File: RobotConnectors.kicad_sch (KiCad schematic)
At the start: 87 parts, among them J1 Conn_02x11_Top_Bottom, J10 Conn_01x05, J11 SA/SC Perimeter Plug, J12 Hall3 (Lift Left), J13 Hall2 (Lift Right), J14 Hall1 (Stop1), J15 Hall0 (Stop2), J17 Conn_01x02, J18 Conn_01x02, J19 Conn_01x04, J2 Conn_02x04_Top_Bottom, J21 Conn_01x05, J27 Rear Stop Switch 2, J3 Conn_01x02, J4 Conn_01x04, J40 Rear Stop Switch 1, J5 OEM CoverUI, J6 Conn_01x14_Socket, J7 USS 1-5, J8 Hall5 (Lift Left 2), J9 Hall4 (Lift Right 2), U11 SN74LVC07ADBR, U12 SN74LVC07ADBR, U14 Fuse Holder, U15 Fuse Holder, U16 Fuse Holder, U17 Fuse Holder, U2 TPS2065CDBV, U28 Fuse 2A, U29 Fuse 2A, U47 SN74LVC157ADR, U48 SN74LVC157ADR

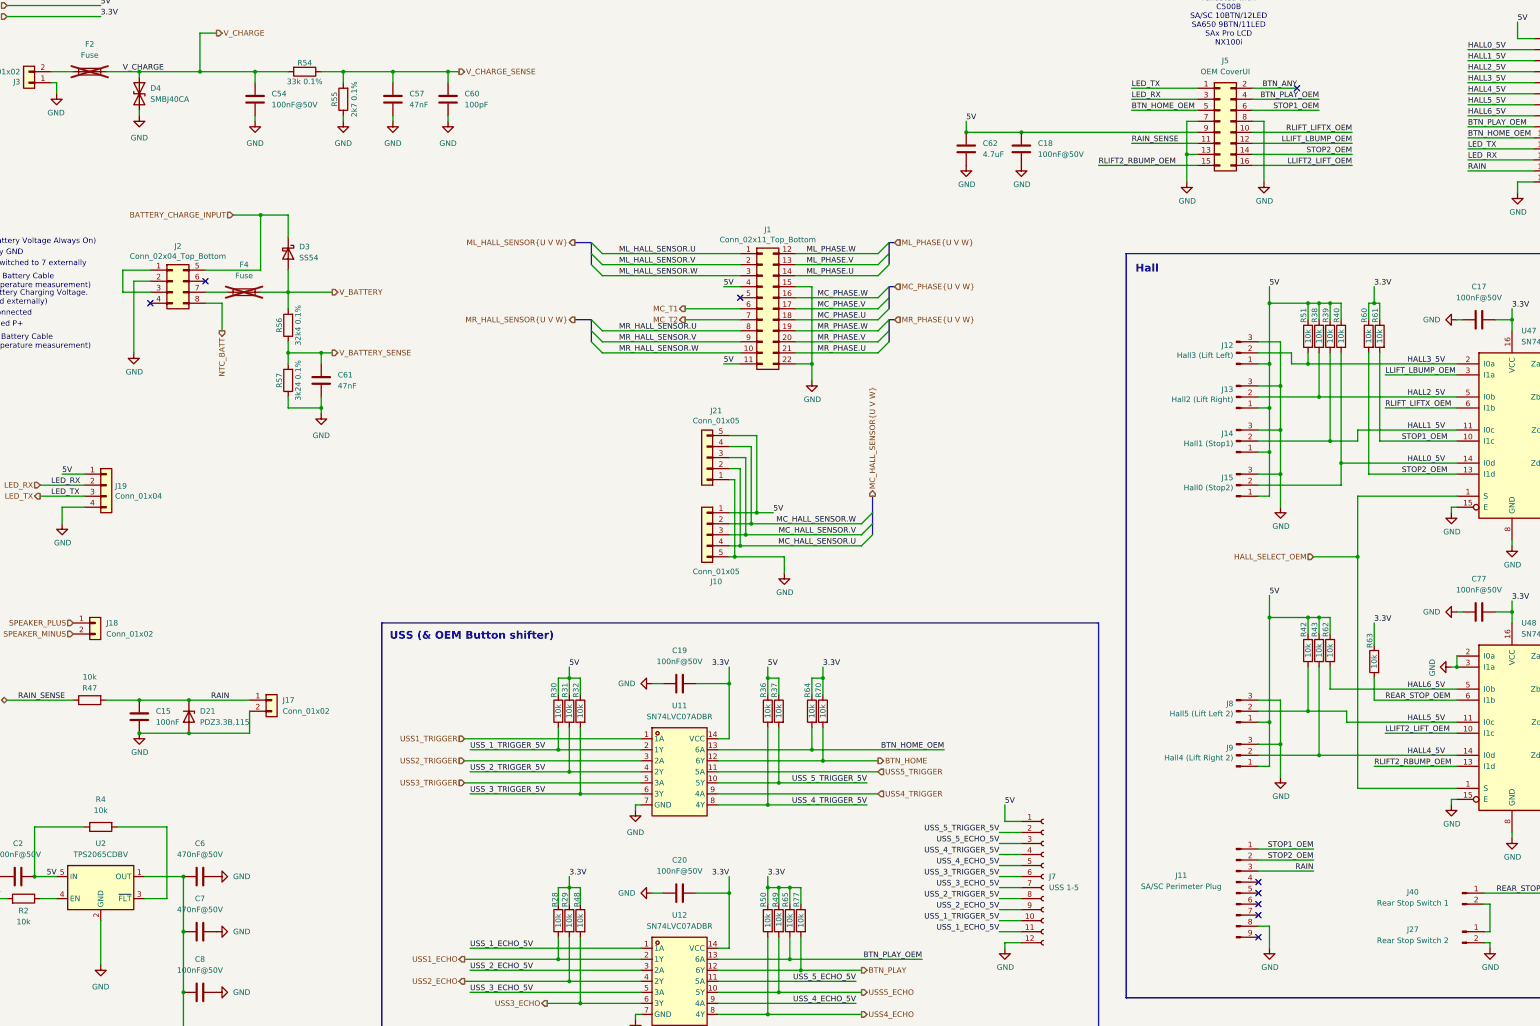
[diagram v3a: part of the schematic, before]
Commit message: Fix BOM and switch C0402 to C0603
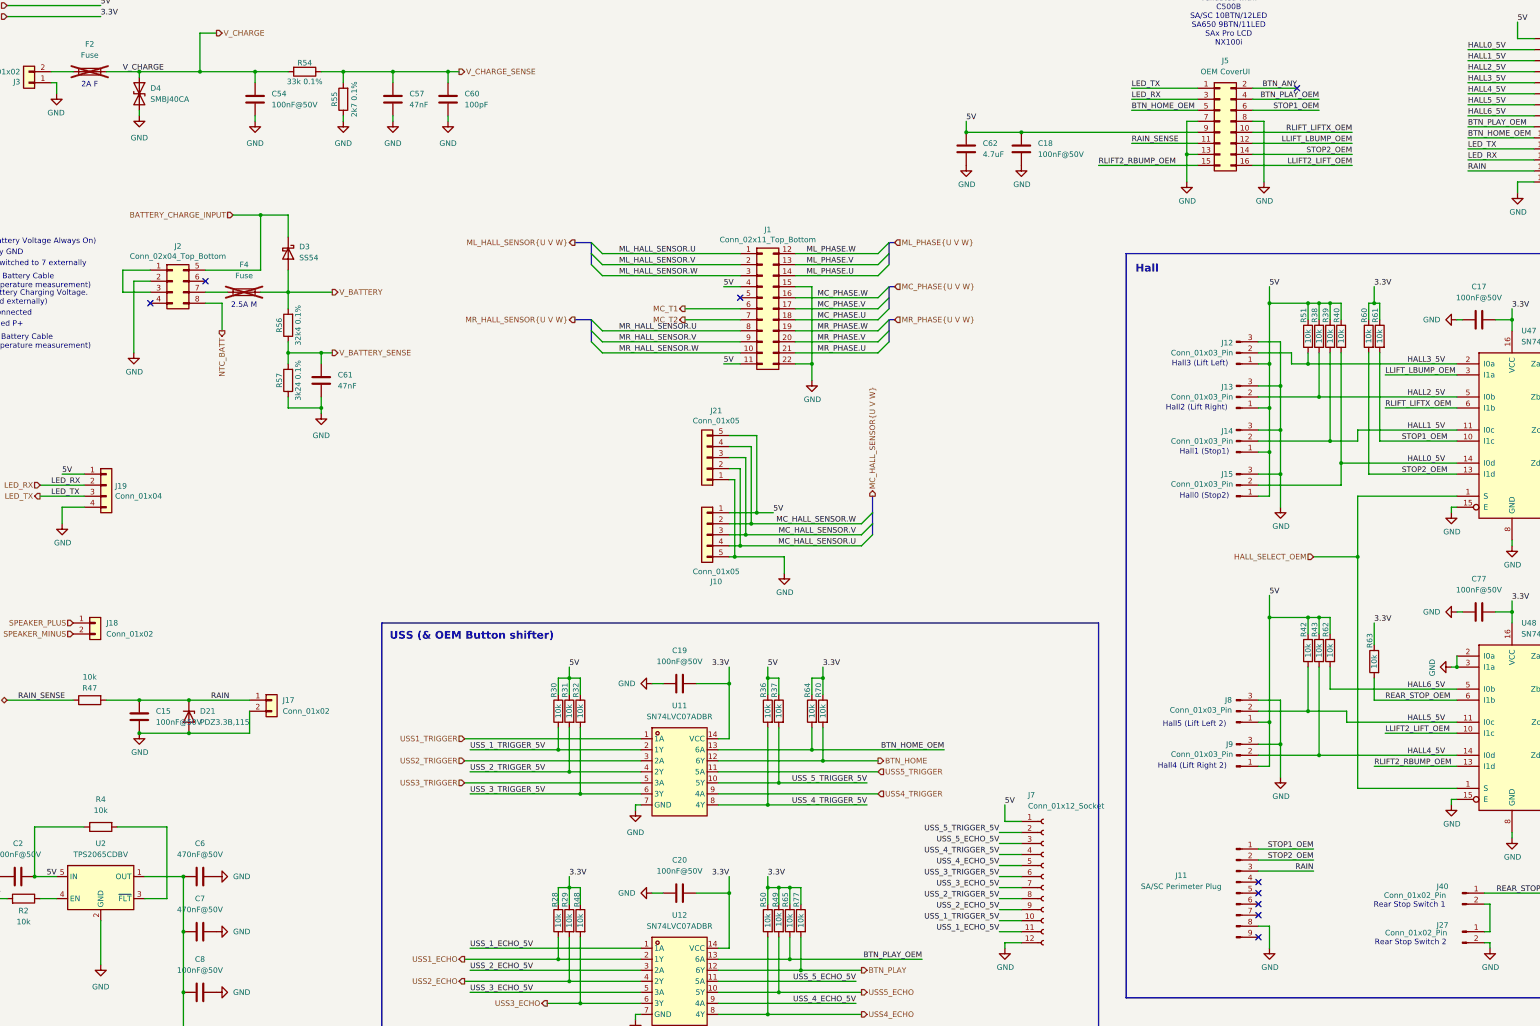
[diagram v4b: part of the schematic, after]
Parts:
- C15: value 100nF -> 100nF@50V; footprint Capacitor_SMD:C_0402_1005Metric -> Capacitor_SMD:C_0603_1608Metric; JLC C307331 -> C14663
- C17, C18, C19, C2, C20, C54, C77, C8: footprint Capacitor_SMD:C_0402_1005Metric -> Capacitor_SMD:C_0603_1608Metric; JLC C307331 -> C14663
- C60: footprint Capacitor_SMD:C_0402_1005Metric -> Capacitor_SMD:C_0603_1608Metric; JLC C1546 -> C14858
- F2, F4: footprint MyModules:Fuseholder5x20_horiz_open_inline_Type-I -> xtech:Fuseholder5x20_horiz_open_inline_XF-003; now left out of the parts list
- J12: value Hall3 (Lift Left) -> Conn_01x03_Pin
- J13: value Hall2 (Lift Right) -> Conn_01x03_Pin
- J14: value Hall1 (Stop1) -> Conn_01x03_Pin
- J15: value Hall0 (Stop2) -> Conn_01x03_Pin
- J27: value Rear Stop Switch 2 -> Conn_01x02_Pin
- J40: value Rear Stop Switch 1 -> Conn_01x02_Pin
- J6: JLC (none) -> C2905420
- J7: value USS 1-5 -> Conn_01x12_Socket; JLC (none) -> C5224029
- J8: value Hall5 (Lift Left 2) -> Conn_01x03_Pin
- J9: value Hall4 (Lift Right 2) -> Conn_01x03_Pin
- R54: footprint Resistor_SMD:R_0402_1005Metric -> Resistor_SMD:R_0603_1608Metric; JLC C5455470 -> C705768
- R55: footprint Resistor_SMD:R_0402_1005Metric -> Resistor_SMD:R_0603_1608Metric; JLC C852706 -> C318131
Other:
- note added: "2.5A M"
- note added: "2A F"
- note added: "Hall0 (Stop2)"
- note added: "Hall1 (Stop1)"
- note added: "Hall2 (Lift Right)"
- note added: "Hall3 (Lift Left)"
- note added: "Hall4 (Lift Right 2)"
- note added: "Hall5 (Lift Left 2)"
- note added: "Rear Stop Switch 1"
- note added: "Rear Stop Switch 2"

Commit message: Switch R0402 to 0603
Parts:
- R2, R28, R29, R30, R31, R32, R36, R37, R38, R39, R4, R40, R42, R43, R47, R48, R49, R50, R51, R60, R61, R62, R63, R64, R65, R70, R77: footprint Resistor_SMD:R_0402_1005Metric -> Resistor_SMD:R_0603_1608Metric; JLC C25744 -> C25804
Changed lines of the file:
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@@
 			)
 		)
-		(property "Footprint" "Resistor_SMD:R_0402_1005Metric"
+		(property "Footprint" "Resistor_SMD:R_0603_1608Metric"
 			(at 344.678 171.45 90)
 			(effects
@@
 			)
 		)
-		(property "JLC" "C25744"
+		(property "JLC" "C25804"
 			(at 342.9 171.45 0)
 			(effects
@@
 			)
 		)
-		(property "Footprint" "Resistor_SMD:R_0402_1005Metric"
+		(property "Footprint" "Resistor_SMD:R_0603_1608Metric"
 			(at 207.518 231.14 90)
 			(effects
@@
 			)
 		)
-		(property "JLC" "C25744"
+		(property "JLC" "C25804"
 			(at 205.74 231.14 0)
 			(effects
@@
 			)
 		)
-		(property "Footprint" "Resistor_SMD:R_0402_1005Metric"
+		(property "Footprint" "Resistor_SMD:R_0603_1608Metric"
 			(at 159.258 231.14 90)
 			(effects
@@
 			)
 		)
-		(property "JLC" "C25744"
+		(property "JLC" "C25804"
 			(at 157.48 231.14 0)
 			(effects
@@
 			)
 		)
-		(property "Footprint" "Resistor_SMD:R_0402_1005Metric"
+		(property "Footprint" "Resistor_SMD:R_0603_1608Metric"
 			(at 49.53 207.772 90)
 			(effects
@@
 			)
 		)
-		(property "JLC" "C25744"
+		(property "JLC" "C25804"
 			(at 49.53 209.55 0)
 			(effects
@@
 			)
 		)
-		(property "Footprint" "Resistor_SMD:R_0402_1005Metric"
+		(property "Footprint" "Resistor_SMD:R_0603_1608Metric"
 			(at 217.678 182.88 90)
 			(effects
@@
 			)
 		)
-		(property "JLC" "C25744"
+		(property "JLC" "C25804"
 			(at 215.9 182.88 0)
 			(effects
@@
 			)
 		)
-		(property "Footprint" "Resistor_SMD:R_0402_1005Metric"
+		(property "Footprint" "Resistor_SMD:R_0603_1608Metric"
 			(at 161.798 182.88 90)
 			(effects
@@
 			)
 		)
-		(property "JLC" "C25744"
+		(property "JLC" "C25804"
 			(at 160.02 182.88 0)
 			(effects
@@
 			)
 		)
-		(property "Footprint" "Resistor_SMD:R_0402_1005Metric"
+		(property "Footprint" "Resistor_SMD:R_0603_1608Metric"
 			(at 345.948 96.52 90)
 			(effects
@@
 			)
 		)
-		(property "JLC" "C25744"
+		(property "JLC" "C25804"
 			(at 344.17 96.52 0)
 			(effects
@@
 			)
 		)
-		(property "Footprint" "Resistor_SMD:R_0402_1005Metric"
+		(property "Footprint" "Resistor_SMD:R_0603_1608Metric"
 			(at 343.408 96.52 90)
 			(effects
@@
 			)
 		)
-		(property "JLC" "C25744"
+		(property "JLC" "C25804"
 			(at 341.63 96.52 0)
 			(effects
@@
 			)
 		)
-		(property "Footprint" "Resistor_SMD:R_0402_1005Metric"
+		(property "Footprint" "Resistor_SMD:R_0603_1608Metric"
 			(at 207.518 182.88 90)
 			(effects
@@
 			)
 		)
-		(property "JLC" "C25744"
+		(property "JLC" "C25804"
 			(at 205.74 182.88 0)
 			(effects
@@
 			)
 		)
-		(property "Footprint" "Resistor_SMD:R_0402_1005Metric"
+		(property "Footprint" "Resistor_SMD:R_0603_1608Metric"
 			(at 161.798 231.14 90)
 			(effects
@@
 			)
 		)
-		(property "JLC" "C25744"
+		(property "JLC" "C25804"
 			(at 160.02 231.14 0)
 			(effects
@@
 			)
 		)
-		(property "Footprint" "Resistor_SMD:R_0402_1005Metric"
+		(property "Footprint" "Resistor_SMD:R_0603_1608Metric"
 			(at 337.058 96.52 90)
 			(effects
@@
 			)
 		)
-		(property "JLC" "C25744"
+		(property "JLC" "C25804"
 			(at 335.28 96.52 0)
 			(effects
@@
 			)
 		)
-		(property "Footprint" "Resistor_SMD:R_0402_1005Metric"
+		(property "Footprint" "Resistor_SMD:R_0603_1608Metric"
 			(at 331.978 168.91 90)
 			(effects
@@
 			)
 		)
-		(property "JLC" "C25744"
+		(property "JLC" "C25804"
 			(at 330.2 168.91 0)
 			(effects
@@
 			)
 		)
-		(property "Footprint" "Resistor_SMD:R_0402_1005Metric"
+		(property "Footprint" "Resistor_SMD:R_0603_1608Metric"
 			(at 215.138 182.88 90)
 			(effects
@@
 			)
 		)
-		(property "JLC" "C25744"
+		(property "JLC" "C25804"
 			(at 213.36 182.88 0)
 			(effects
@@
 			)
 		)
-		(property "Footprint" "Resistor_SMD:R_0402_1005Metric"
+		(property "Footprint" "Resistor_SMD:R_0603_1608Metric"
 			(at 212.598 231.14 90)
 			(effects
@@
 			)
 		)
-		(property "JLC" "C25744"
+		(property "JLC" "C25804"
 			(at 210.82 231.14 0)
 			(effects
@@
 			)
 		)
-		(property "Footprint" "Resistor_SMD:R_0402_1005Metric"
+		(property "Footprint" "Resistor_SMD:R_0603_1608Metric"
 			(at 159.258 182.88 90)
 			(effects
@@
 			)
 		)
-		(property "JLC" "C25744"
+		(property "JLC" "C25804"
 			(at 157.48 182.88 0)
 			(effects
@@
 			)
 		)
-		(property "Footprint" "Resistor_SMD:R_0402_1005Metric"
+		(property "Footprint" "Resistor_SMD:R_0603_1608Metric"
 			(at 156.718 231.14 90)
 			(effects
@@
 			)
 		)
-		(property "JLC" "C25744"
+		(property "JLC" "C25804"
 			(at 154.94 231.14 0)
 			(effects
@@
 			)
 		)
-		(property "Footprint" "Resistor_SMD:R_0402_1005Metric"
+		(property "Footprint" "Resistor_SMD:R_0603_1608Metric"
 			(at 329.438 96.52 90)
 			(effects
@@
 			)
 		)
-		(property "JLC" "C25744"
+		(property "JLC" "C25804"
 			(at 327.66 96.52 0)
 			(effects
@@
 			)
 		)
-		(property "Footprint" "Resistor_SMD:R_0402_1005Metric"
+		(property "Footprint" "Resistor_SMD:R_0603_1608Metric"
 			(at 204.978 182.88 90)
 			(effects
@@
 			)
 		)
-		(property "JLC" "C25744"
+		(property "JLC" "C25804"
 			(at 203.2 182.88 0)
 			(effects
@@
 			)
 		)
-		(property "Footprint" "Resistor_SMD:R_0402_1005Metric"
+		(property "Footprint" "Resistor_SMD:R_0603_1608Metric"
 			(at 204.978 231.14 90)
 			(effects
@@
 			)
 		)
-		(property "JLC" "C25744"
+		(property "JLC" "C25804"
 			(at 203.2 231.14 0)
 			(effects
@@
 			)
 		)
-		(property "Footprint" "Resistor_SMD:R_0402_1005Metric"
+		(property "Footprint" "Resistor_SMD:R_0603_1608Metric"
 			(at 210.058 231.14 90)
 			(effects
@@
 			)
 		)
-		(property "JLC" "C25744"
+		(property "JLC" "C25804"
 			(at 208.28 231.14 0)
 			(effects
@@
 			)
 		)
-		(property "Footprint" "Resistor_SMD:R_0402_1005Metric"
+		(property "Footprint" "Resistor_SMD:R_0603_1608Metric"
 			(at 334.518 96.52 90)
 			(effects
@@
 			)
 		)
-		(property "JLC" "C25744"
+		(property "JLC" "C25804"
 			(at 332.74 96.52 0)
 			(effects
@@
 			)
 		)
-		(property "Footprint" "Resistor_SMD:R_0402_1005Metric"
+		(property "Footprint" "Resistor_SMD:R_0603_1608Metric"
 			(at 156.718 182.88 90)
 			(effects
@@
 			)
 		)
-		(property "JLC" "C25744"
+		(property "JLC" "C25804"
 			(at 154.94 182.88 0)
 			(effects
@@
 			)
 		)
-		(property "Footprint" "Resistor_SMD:R_0402_1005Metric"
+		(property "Footprint" "Resistor_SMD:R_0603_1608Metric"
 			(at 331.978 96.52 90)
 			(effects
@@
 			)
 		)
-		(property "JLC" "C25744"
+		(property "JLC" "C25804"
 			(at 330.2 96.52 0)
 			(effects
@@
 			)
 		)
-		(property "Footprint" "Resistor_SMD:R_0402_1005Metric"
+		(property "Footprint" "Resistor_SMD:R_0603_1608Metric"
 			(at 334.518 168.91 90)
 			(effects
@@
 			)
 		)
-		(property "JLC" "C25744"
+		(property "JLC" "C25804"
 			(at 332.74 168.91 0)
 			(effects
@@
 			)
 		)
-		(property "Footprint" "Resistor_SMD:R_0402_1005Metric"
+		(property "Footprint" "Resistor_SMD:R_0603_1608Metric"
 			(at 329.438 168.91 90)
 			(effects
@@
 			)
 		)
-		(property "JLC" "C25744"
+		(property "JLC" "C25804"
 			(at 327.66 168.91 0)
 			(effects
@@
 			)
 		)
-		(property "Footprint" "Resistor_SMD:R_0402_1005Metric"
+		(property "Footprint" "Resistor_SMD:R_0603_1608Metric"
 			(at 46.99 178.562 90)
 			(effects
@@
 			)
 		)
-		(property "JLC" "C25744"
+		(property "JLC" "C25804"
 			(at 46.99 180.34 0)
 			(effects
@@
 			)
 		)
-		(property "Footprint" "Resistor_SMD:R_0402_1005Metric"
+		(property "Footprint" "Resistor_SMD:R_0603_1608Metric"
 			(at 31.75 227.838 90)
 			(effects
@@
 			)
 		)
-		(property "JLC" "C25744"
+		(property "JLC" "C25804"
 			(at 31.75 226.06 0)
 			(effects

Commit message: Fix BOM and parts placement
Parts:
- J10, J17, J18, J19, J21, J4: FT Rotation Offset (none) -> 180
- J5: JLC C601981 -> C3406
- J6, J7, U2: FT Rotation Offset (none) -> 90
- U14, U15, U16, U17: JLC C206977 -> C717027
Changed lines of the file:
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@@
 			)
 		)
-		(property "JLC" "C601981"
+		(property "JLC" "C3406"
 			(at 307.34 46.99 0)
 			(effects
@@
 			)
 		)
-		(property "APPLICATION" ""
+		(property "FT Rotation Offset" "180"
 			(at 189.23 124.46 0)
 			(effects
@@
 			)
 		)
-		(property "APPLICATION" ""
+		(property "FT Rotation Offset" "180"
 			(at 50.8 130.81 0)
 			(effects
@@
 			)
 		)
-		(property "JLC" "C206977"
+		(property "JLC" "C717027"
 			(at 179.07 -20.32 0)
 			(effects
@@
 			)
 		)
-		(property "JLC" "C206977"
+		(property "JLC" "C717027"
 			(at 179.07 -2.54 0)
 			(effects
@@
 			)
 		)
-		(property "JLC" "C206977"
+		(property "JLC" "C717027"
 			(at 179.07 -11.43 0)
 			(effects
@@
 			)
 		)
-		(property "APPLICATION" ""
+		(property "FT Rotation Offset" "180"
 			(at 88.9 180.34 0)
 			(effects
@@
 			)
 		)
+		(property "FT Rotation Offset" "90"
+			(at 384.81 43.18 0)
+			(effects
+				(font
+					(size 1.27 1.27)
+				)
+				(hide yes)
+			)
+		)
 		(pin "1"
 		)
@@
 			)
 		)
-		(property "APPLICATION" ""
+		(property "FT Rotation Offset" "90"
 			(at 49.53 223.52 0)
 			(effects
@@
 			)
 		)
-		(property "JLC" "C206977"
+		(property "JLC" "C717027"
 			(at 179.07 -29.21 0)
 			(effects
@@
 			)
 		)
-		(property "APPLICATION" ""
+		(property "FT Rotation Offset" "180"
 			(at 45.72 264.16 0)
 			(effects
@@
 			)
 		)
-		(property "APPLICATION" ""
+		(property "FT Rotation Offset" "180"
 			(at 189.23 142.24 0)
 			(effects
@@
 			)
 		)
+		(property "FT Rotation Offset" "90"
+			(at 266.7 220.98 0)
+			(effects
+				(font
+					(size 1.27 1.27)
+				)
+				(hide yes)
+			)
+		)
 		(pin "1"
 		)
@@
 			)
 		)
-		(property "APPLICATION" ""
+		(property "FT Rotation Offset" "180"
 			(at 48.26 162.56 0)
 			(effects
